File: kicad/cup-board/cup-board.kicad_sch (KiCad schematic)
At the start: 13 parts, among them J2 EARCUP_SPKR_R, J3 CUP_PWR_IN, U1 ADAU1861, U2 LSM6DSV16BX

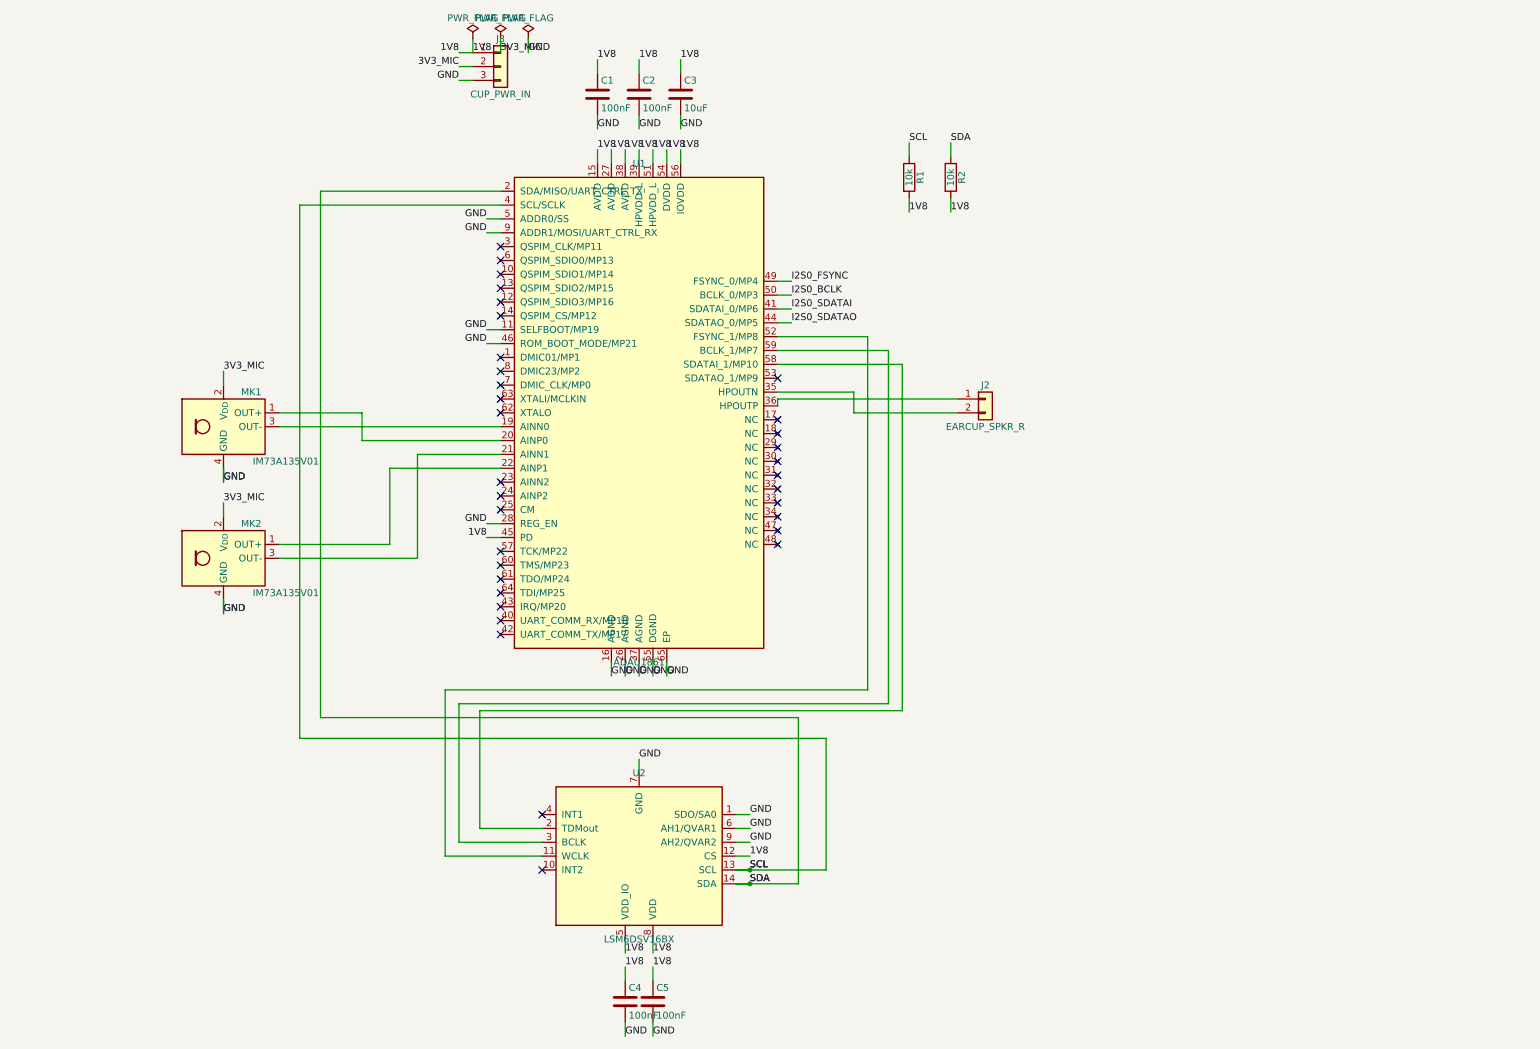
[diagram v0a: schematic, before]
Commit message: [LIMA] unify cup A/B into one cup-board: ADAU1861, 3x IM73A135, LSM6DSV16BX on TDM, per Peter
Both earcups are now identical, so one schematic fitted twice replaces
cup-a-board (891d746) and cup-b-board (7ffb480), removed here and kept in
history. FF/FB ANC mics on ADC0/ADC1, a third IM73A135 as the voice mic
on ADC2 in place of the boom mic, and the LSM6DSV16BX as DVNC reference
over TDM into SPT1. All three inputs are differential, so CM is now NC.

Departs from Rev G's per-cup slot map (boom on cup A ADC2, accel on cup B
ADC2); the A2B upstream allocation needs revisiting - recorded in the
README with the other open items (shared I2C address on identical cups,
SPT1 as TDM clock master, no A2B subnode/power/footprints yet).

I2C and TDM now join by net labels instead of long wires, which removes
the wire-through-symbol and grid-snap-short problems hit on cup-b-board.
ERC 0 errors; every unnamed net checked pin-by-pin in the kicad-cli
netlist (MKn OUT+/- -> AINPn/AINNn, J2.1 -> HPOUTN, J2.2 -> HPOUTP).

Co-Authored-By: Claude Opus 5.5 <noreply@anthropic.com>
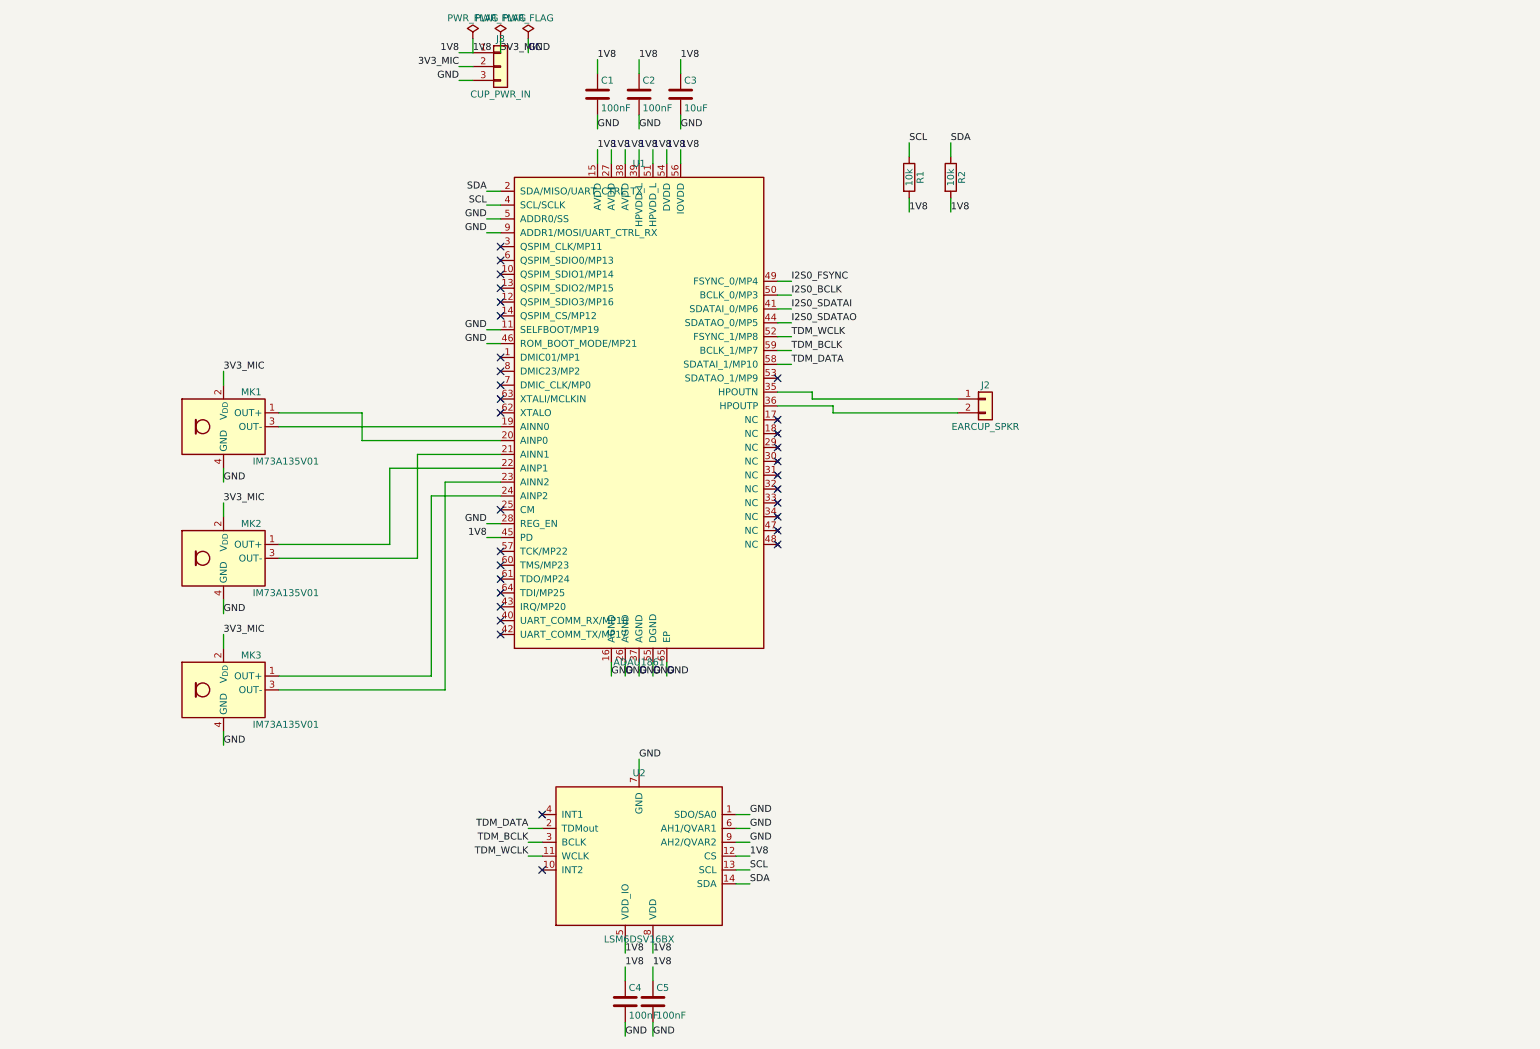
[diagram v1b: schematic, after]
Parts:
- added MK3: IM73A135V01, symbol Sensor_Audio:IM73A135V01
- J2: value EARCUP_SPKR_R -> EARCUP_SPKR
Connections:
- net 3V3_MIC: now also MK3.2 (V_{DD})
- net GND: now also MK3.4 (GND), MK3.5 (GND)
- net TDM_WCLK: now reaches U1.52 (FSYNC_1/MP8), U2.11 (WCLK)
- net TDM_DATA: now reaches U1.58 (SDATAI_1/MP10), U2.2 (TDMout)
- net TDM_BCLK: now reaches U1.59 (BCLK_1/MP7), U2.3 (BCLK)
- net at J2.1 (Pin_1): now also U1.35 (HPOUTN); no longer U1.36 (HPOUTP)
- net at J2.2 (Pin_2): now also U1.36 (HPOUTP); no longer U1.35 (HPOUTN)
- net at U1.23 (AINN2): now also MK3.3 (OUT-)
- net at U1.24 (AINP2): now also MK3.1 (OUT+)
- no-connect marks 34 -> 32

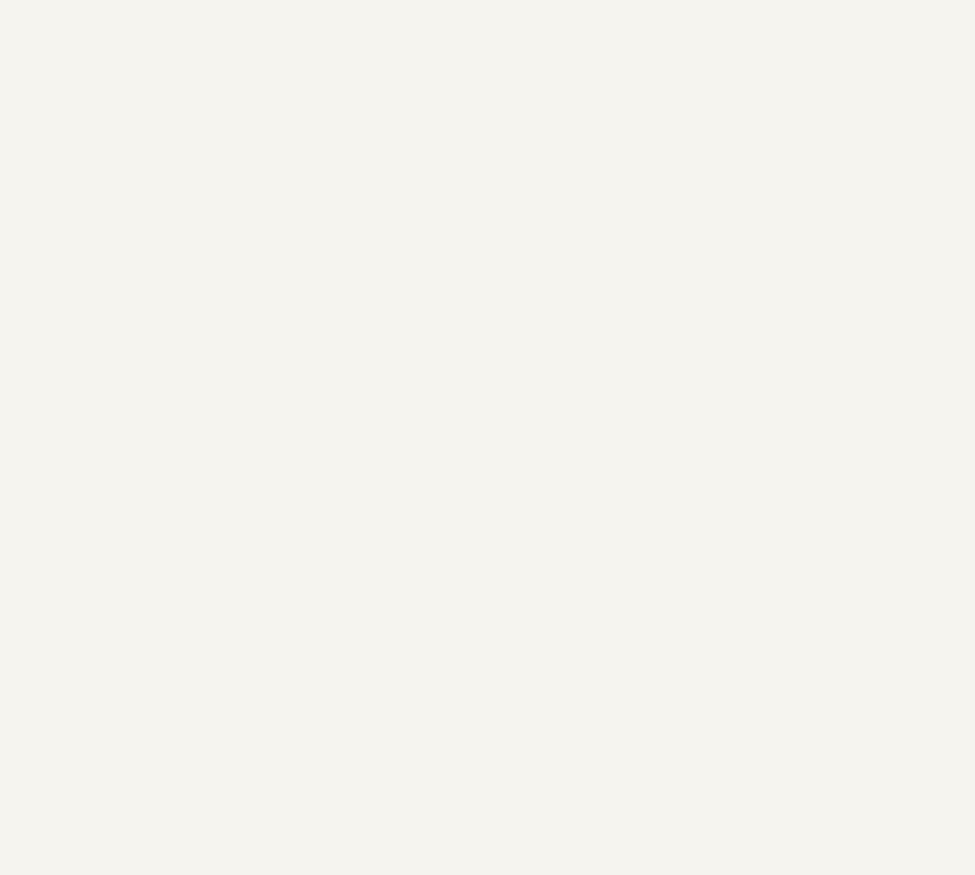
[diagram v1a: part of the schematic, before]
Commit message: [LIMA] add MAXM86161 HR/SpO2 module to cup-board, per Peter
U3 on the shared I2C bus (fixed address 0x62, no clash with the ADAU1861
at 0x64 or the LSM6DSV16BX), INTB pulled up by R3 and brought out as
PPG_INT, LDO_EN tied to 1V8, GPIO and the LED-cathode pins 6/7/8 left
unconnected per the datasheet. VLDO/VREF get 1uF each and VLED 10uF.

VLED gets its own connector (J4) rather than sharing 3V3_MIC: the LED
driver pulses up to 124 mA, which would land on the bias supply of all
three mics. VLED voltage (datasheet range 3.0-5.5 V) is still open, as
are where PPG_INT goes and power-up sequencing - all in the README.

New MAXM86161 symbol in kicad/lib/AnalogDevices.kicad_sym, entered from
the datasheet pin table. ERC 0 errors; every new net checked in the
kicad-cli netlist.

Co-Authored-By: Claude Opus 5.5 <noreply@anthropic.com>
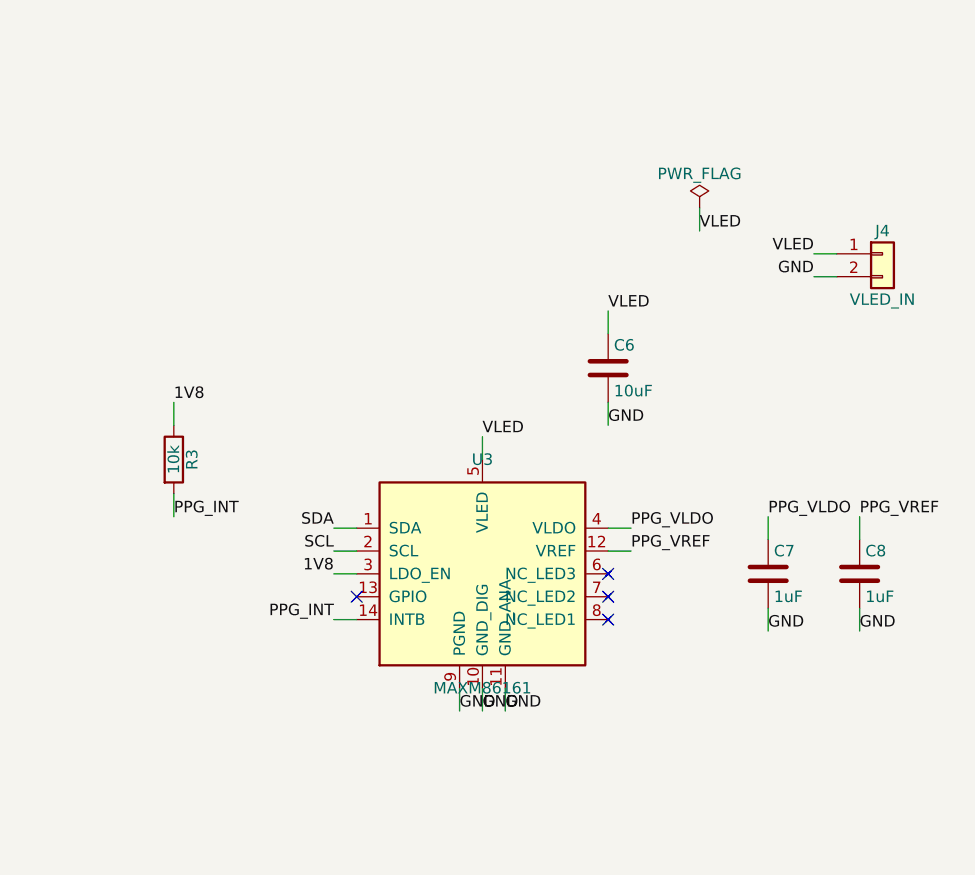
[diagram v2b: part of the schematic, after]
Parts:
- added C6: 10uF, symbol Device:C
- added C7, C8: 1uF, symbol Device:C
- added J4: VLED_IN, symbol Connector_Generic:Conn_01x02
- added R3: 10k, symbol Device:R
- added U3: MAXM86161, symbol AnalogDevices:MAXM86161
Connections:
- net 1V8: now also R3.1, U3.3 (LDO_EN)
- net GND: now also C6.2, C7.2, C8.2, J4.2 (Pin_2), U3.10 (GND_DIG), U3.11 (GND_ANA), U3.9 (PGND)
- net SCL: now also U3.2 (SCL)
- net SDA: now also U3.1 (SDA)
- new net PPG_INT: R3.2, U3.14 (INTB)
- new net PPG_VLDO: C7.1, U3.4 (VLDO)
- new net PPG_VREF: C8.1, U3.12 (VREF)
- new net VLED: C6.1, J4.1 (Pin_1), U3.5 (VLED)
- no-connect marks 32 -> 36

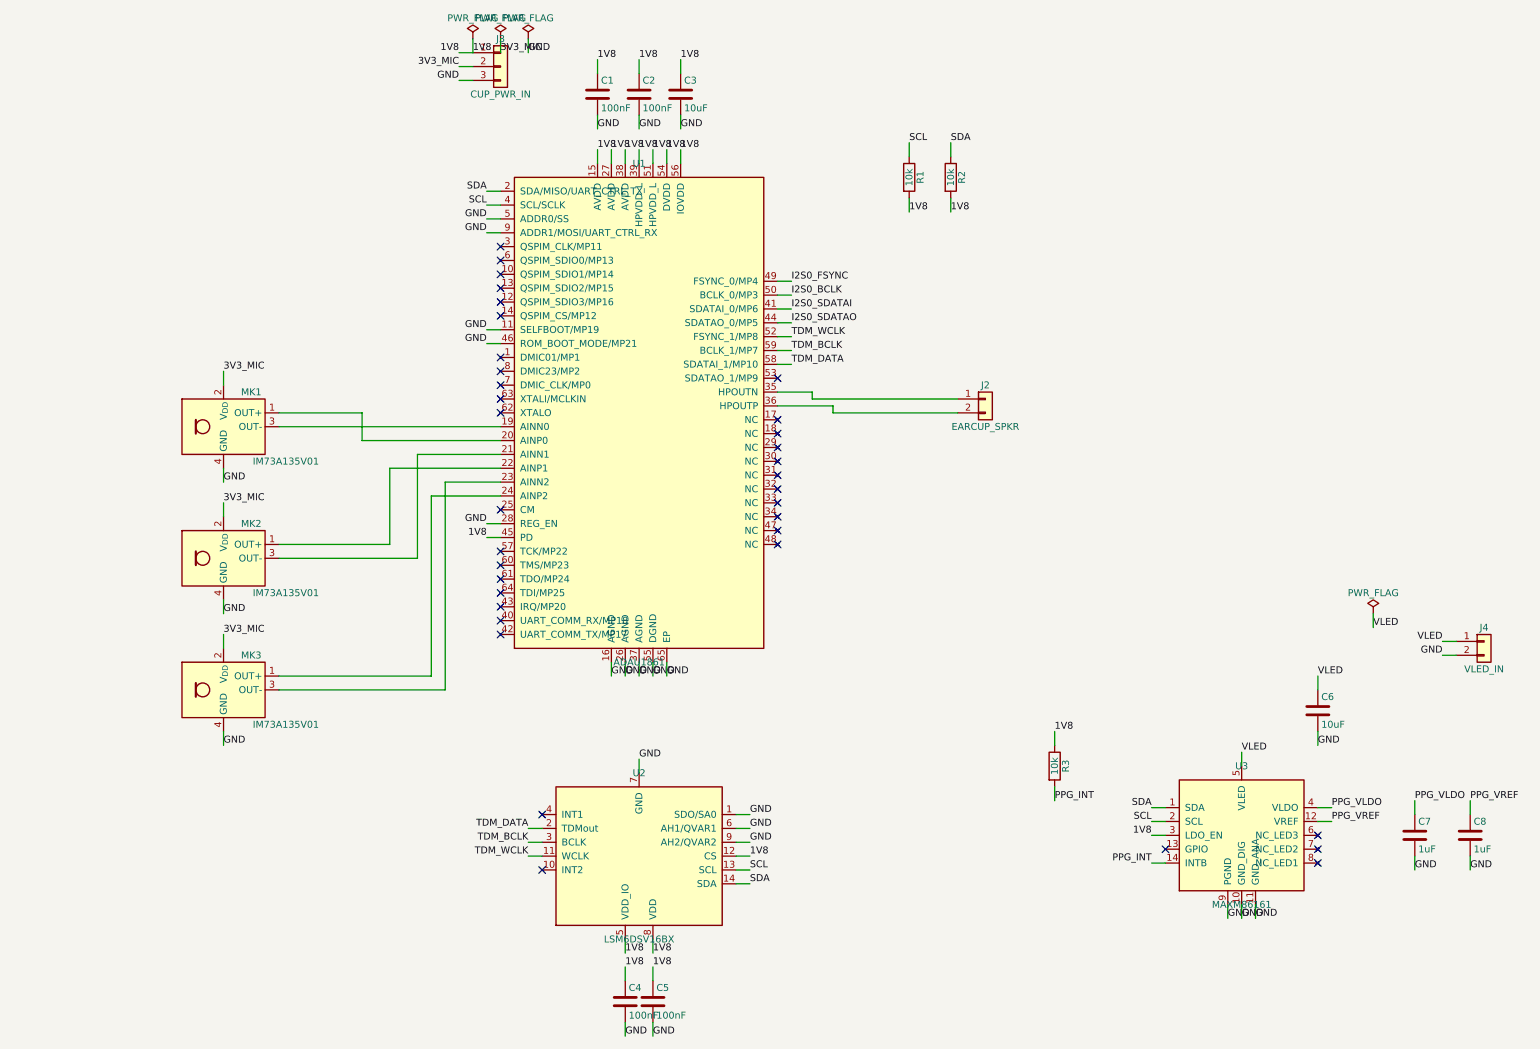
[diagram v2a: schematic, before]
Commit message: [LIMA] cup-board: aircraft audio into ADC2 via SP-74, fail-passive DPDT bypass, per Peter
MK3 removed. J5 aircraft line -> T1 SP-74 (full primary, secondaries parallel, 3.143:1).
K1 G6K-2F-Y DC5: unpowered NC = speaker on T1 secondary (32 ohm reflects to ~316 ohm,
two cups ~158 ohm, inside the panel's >=150 ohm rating); energised NO = HPOUTN/HPOUTP.
The ADC2 tap is taken off the isolated secondary (10k/10k/22k, 0 dBFS at ~7.6 Vrms line).
Coil from upstream on J6 with D1 flyback.

ERC 0 errors (same 8 warnings), 0 shorts, 0 overlaps; every new net checked in the netlist.
Open: SP-74 polarity/pinout, core level at full volume, 100 mW coil per cup, who drives J6.

Co-Authored-By: Claude Opus 5.5 <noreply@anthropic.com>
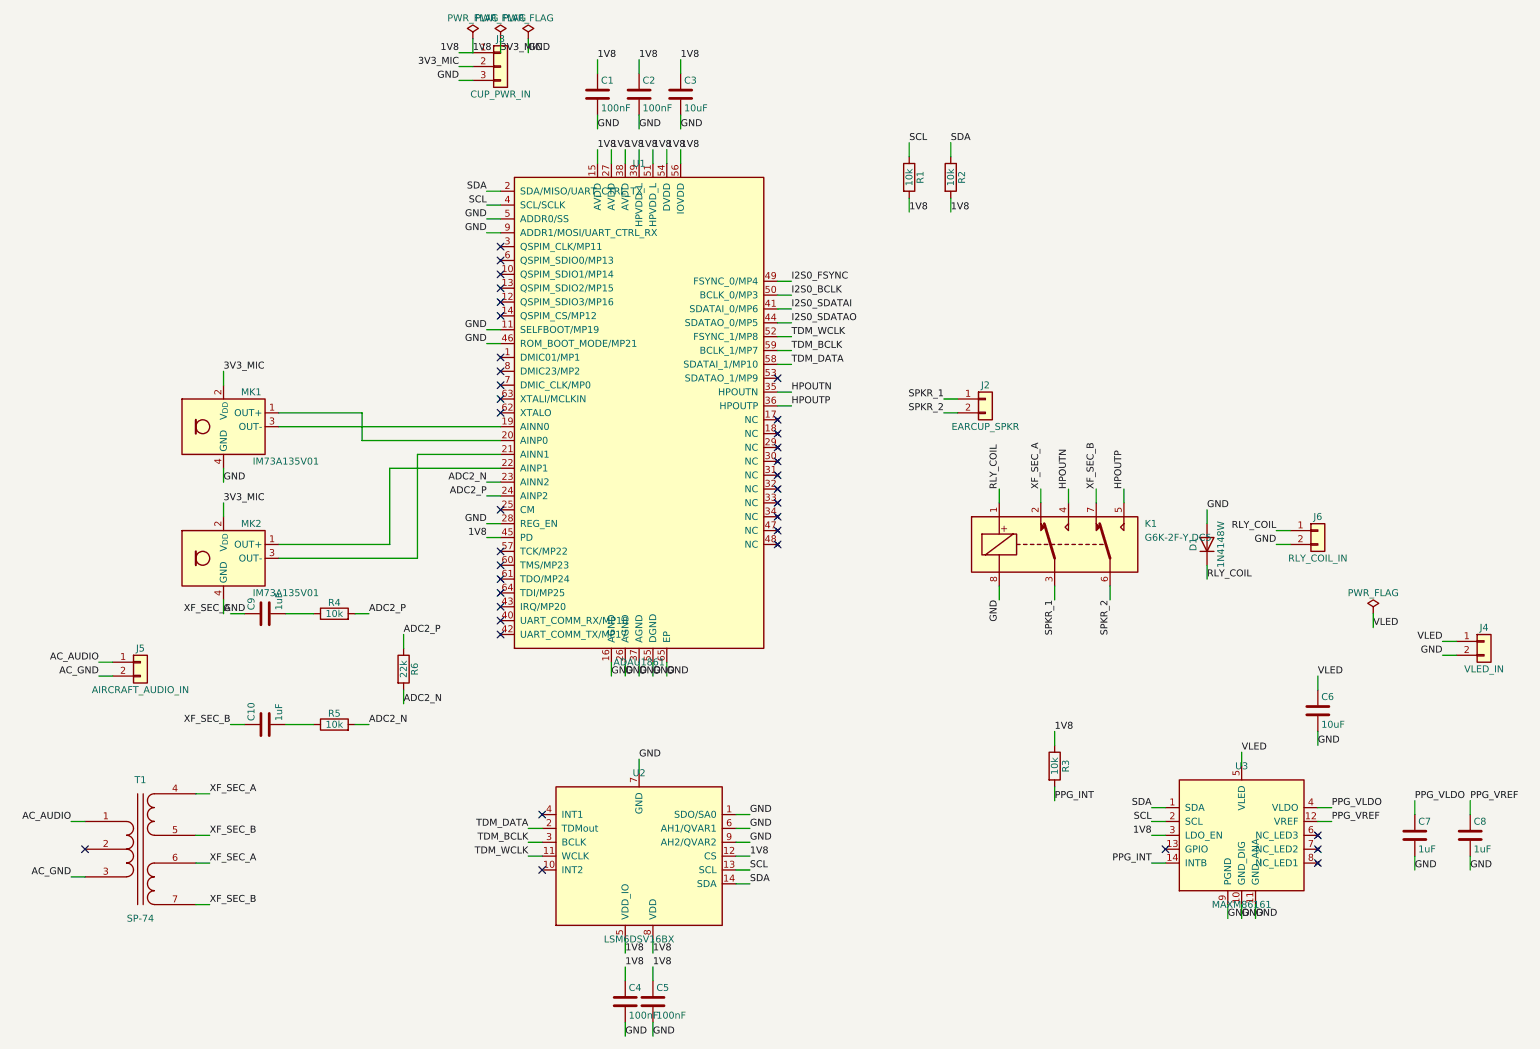
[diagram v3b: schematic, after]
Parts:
- removed MK3: IM73A135V01, symbol Sensor_Audio:IM73A135V01
- added C10, C9: 1uF, symbol Device:C
- added D1: 1N4148W, symbol Device:D
- added J5: AIRCRAFT_AUDIO_IN, symbol Connector_Generic:Conn_01x02
- added J6: RLY_COIL_IN, symbol Connector_Generic:Conn_01x02
- added K1: G6K-2F-Y DC5, symbol Relay:G6K-2
- added R4, R5: 10k, symbol Device:R
- added R6: 22k, symbol Device:R
- added T1: SP-74, symbol Device:Transformer_SP_2S
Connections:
- net GND: now also D1.2 (A), J6.2 (Pin_2), K1.8
- net HPOUTN: now reaches U1.35 (HPOUTN)
- net HPOUTN: now also K1.4; no longer J2.1 (Pin_1)
- net HPOUTP: now reaches U1.36 (HPOUTP)
- net HPOUTP: now also K1.5; no longer J2.2 (Pin_2)
- net ADC2_P: now reaches U1.24 (AINP2)
- net ADC2_P: now also R4.2, R6.1
- net ADC2_N: now reaches U1.23 (AINN2)
- net ADC2_N: now also R5.2, R6.2
- new net: C9.2, R4.1
- new net: C10.2, R5.1
- new net AC_AUDIO: J5.1 (Pin_1), T1.1 (IN+)
- new net AC_GND: J5.2 (Pin_2), T1.3 (IN-)
- new net RLY_COIL: D1.1 (K), J6.1 (Pin_1), K1.1
- new net SPKR_1: J2.1 (Pin_1), K1.3
- new net SPKR_2: J2.2 (Pin_2), K1.6
- new net XF_SEC_A: C9.1, K1.2, T1.4 (OUT1A), T1.6 (OUT2A)
- new net XF_SEC_B: C10.1, K1.7, T1.5 (OUT1B), T1.7 (OUT2B)
- no-connect marks 36 -> 37
